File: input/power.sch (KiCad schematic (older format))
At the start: 61 parts, among them Q2 2STD1665T4, Q3 NSS1C300ET4G, U4 OPA830, U6 OPA830, U7 MCP1755S-3302E/DB, U8 NCP1117STAT3G

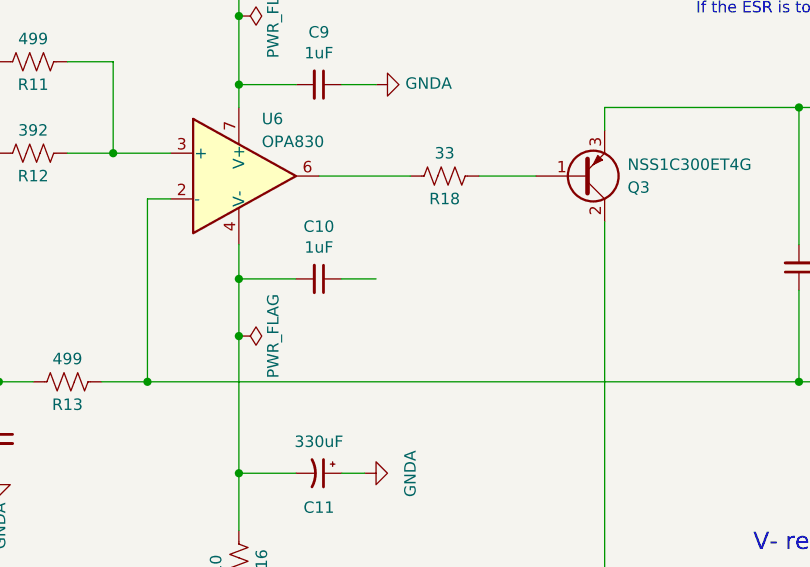
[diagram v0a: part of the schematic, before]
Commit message: Input board is nearly ready to send off for the first spin.
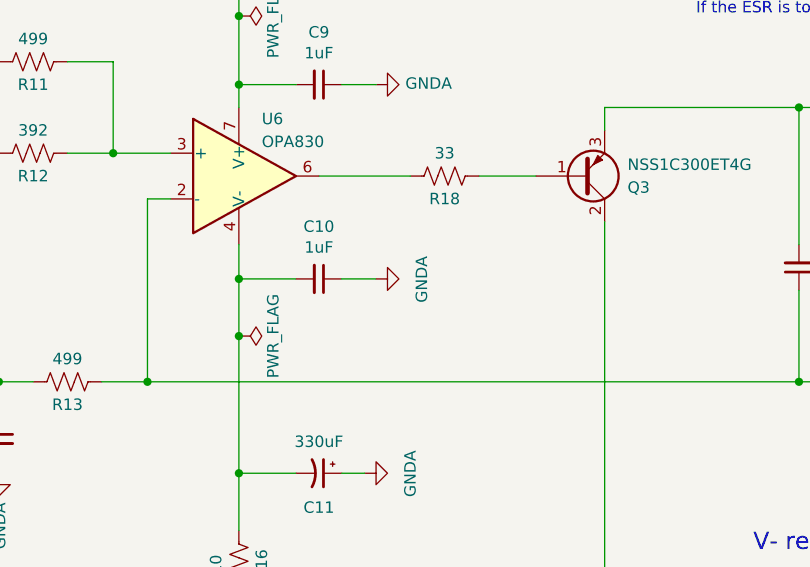
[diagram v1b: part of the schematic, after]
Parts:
- TP4: DK line (none) -> 33; Description (none) -> TERM TURRET HOLLOW L=6.75MM TIN; Digikey (none) -> 36-1540-2-ND; MPN (none) -> 1540-2; Manufacturer (none) -> Keystone Electronics
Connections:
- net GND: now also C10.1
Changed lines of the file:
@@
 $Descr B 17000 11000
 encoding utf-8
-Sheet 11 21
+Sheet 4 21
 Title ""
 Date ""
@@
 F 2 "input:TestPoint_THTPad_D5.0mm_Drill2.41mm" H 2950 8300 50  0001 C CNN
 F 3 "~" H 2950 8300 50  0001 C CNN
+F 4 "33" H 2750 8300 50  0001 C CNN "DK line"
+F 5 "TERM TURRET HOLLOW L=6.75MM TIN" H 2750 8300 50  0001 C CNN "Description"
+F 6 "36-1540-2-ND" H 2750 8300 50  0001 C CNN "Digikey"
+F 7 "1540-2" H 2750 8300 50  0001 C CNN "MPN"
+F 8 "Keystone Electronics" H 2750 8300 50  0001 C CNN "Manufacturer"
 	1    2750 8300
 	1    0    0    -1
@@
 Wire Wire Line
 	7250 2100 7350 2100
+$Comp
+L power:GNDA #PWR?
+U 1 1 5E478F7A
+P 9250 6000
+AR Path="/5DFF6C0D/5E478F7A" Ref="#PWR?"  Part="1"
+AR Path="/5E1D6729/5E1DA2AA/5E478F7A" Ref="#PWR?"  Part="1"
+AR Path="/5E2EB92B/5E478F7A" Ref="#PWR?"  Part="1"
+AR Path="/5E51E83D/5E478F7A" Ref="#PWR0166"  Part="1"
+F 0 "#PWR0166" H 9250 5750 50  0001 C CNN
+F 1 "GNDA" H 9350 5800 50  0000 R CNN
+F 2 "" H 9250 6000 50  0001 C CNN
+F 3 "" H 9250 6000 50  0001 C CNN
+	1    9250 6000
+	0    -1   -1   0
+$EndComp
 $EndSCHEMATC

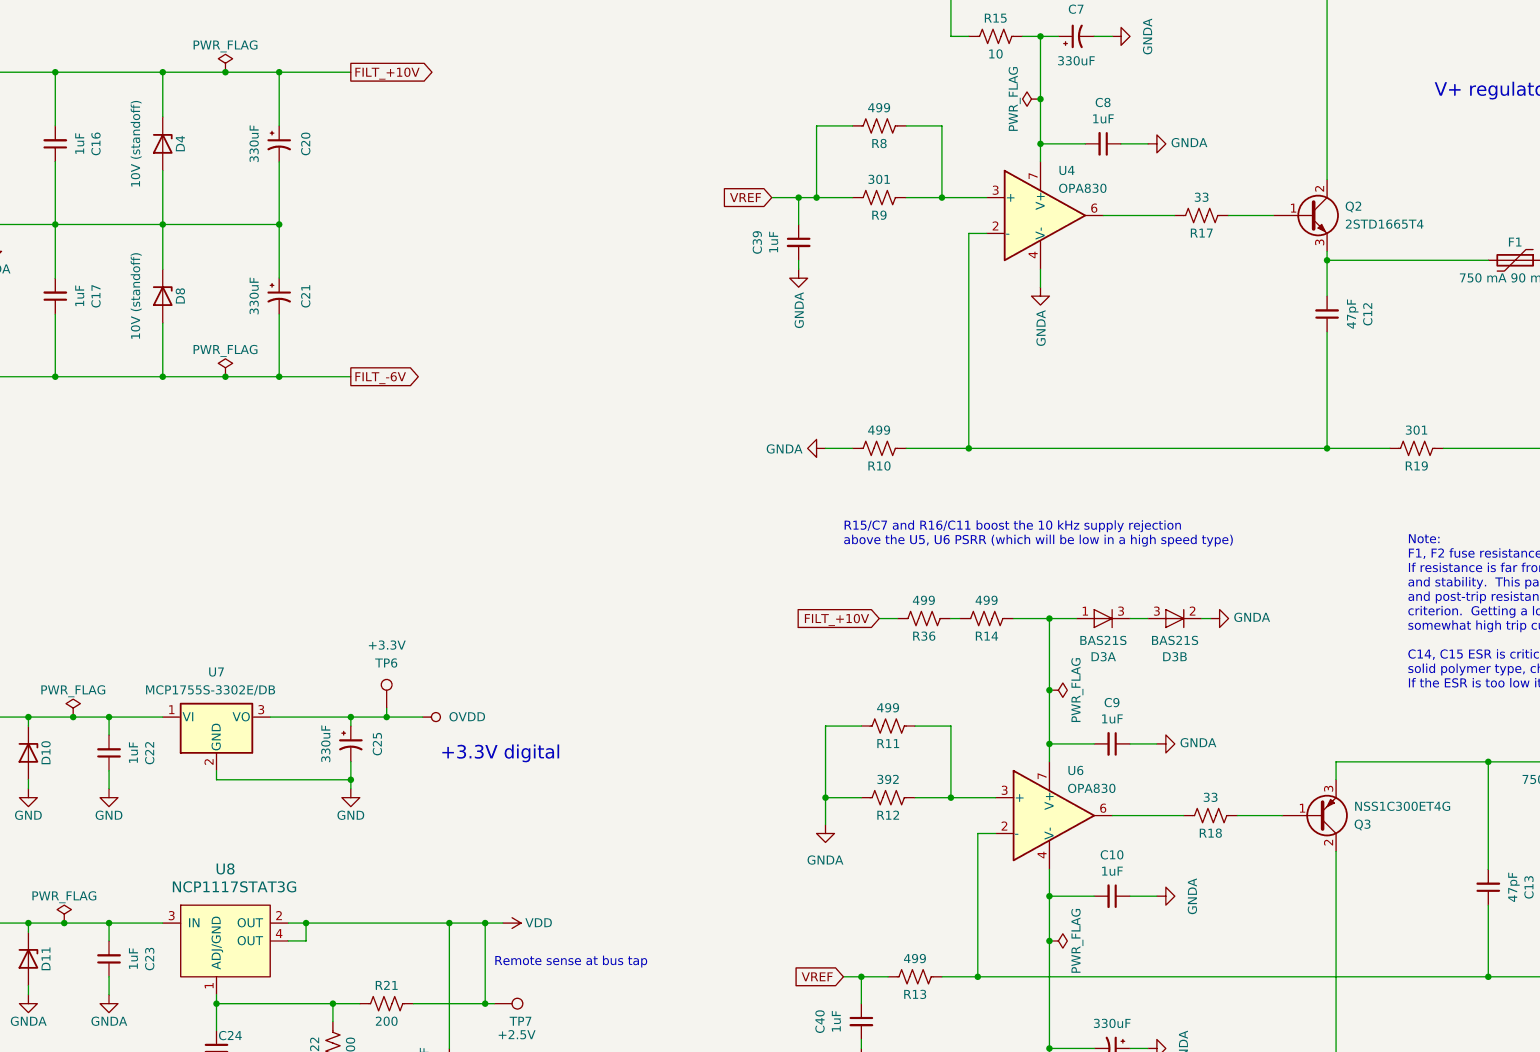
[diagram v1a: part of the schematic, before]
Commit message: Various tweaks to schematic which help in the PCB view, mainly getting informative net names. Also unscrambled the + and - paths in the input channel.  This avoided a cross-over before the first stage, and an unintended inversion, but mostly just made net naming less confusing.
Getting better net names made it easier to review the PCB to see if it made sense.  I checked
the ICs on the PCB against the datasheet pinout, and while doing this fixed an actual bug where
I had BIST-+ and BIST+-swapped.

I made some tweaks on the PCB to try to equalize the copper area on the input nets so as to
match the capacitance.  I tweaked the top-side ground pours somewhat, adding in the regulator
area, removing around the high speed traces.

Some changes from gerber viewing.  I reduced the solder mask clearances so that we get mask
web between the SOIC and DFN pads.  I reduced the pad size of the big via from 1.2 to 1.0 mm.
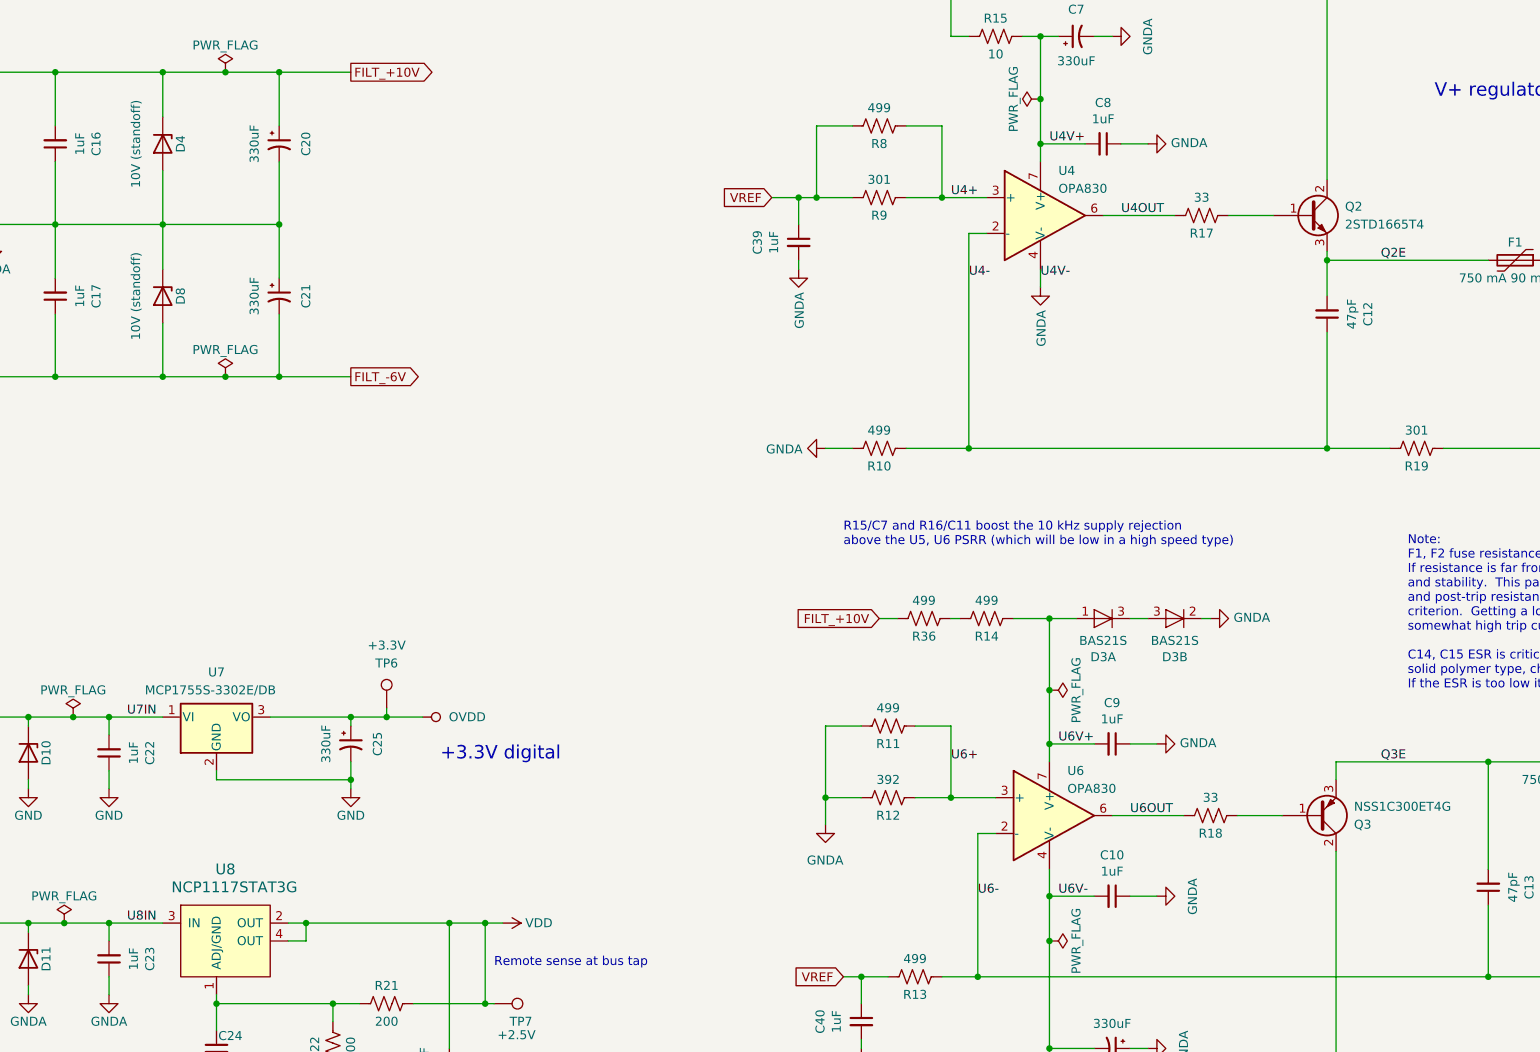
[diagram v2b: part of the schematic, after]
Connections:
- net U6V+: now reaches C9.2, D3.1 (A), R14.1, U6.7 (V+)
- net U8IN: now reaches C23.2, D11.1 (K), FB4.2, U8.3 (IN)
- net U7IN: now reaches C22.2, D10.1 (K), FB3.2, U7.1 (VI)
- net U6-: now reaches C13.1, R13.1, R20.2, U6.2 (-)
- net Q3E: now reaches C13.2, F2.2, Q3.3 (E)
- net U6+: now reaches R11.1, R12.1, U6.3 (+)
- net U6V-: now reaches C10.2, C11.2, R16.1, U6.4 (V-)
- net U6OUT: now reaches R18.2, U6.6
- net U4V+: now reaches C7.1, C8.2, R15.2, U4.7 (V+)
- net U4-: now reaches C12.1, R10.1, R19.2, U4.2 (-)
- net U4+: now reaches R8.1, R9.1, U4.3 (+)
- net U4OUT: now reaches R17.2, U4.6
- net Q2E: now reaches C12.2, F1.2, Q2.3 (E)
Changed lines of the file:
@@
 F 1 "BAS21S" H 8950 4574 50  0000 C CNN
 F 2 "Package_TO_SOT_SMD:SOT-23" H 8950 4300 50  0001 C CNN
-F 3 "https://assets.nexperia.com/documents/data-sheet/BAV99_SER.pdf" H 8950 4550 50  0001 C CNN
+F 3 "http://www.onsemi.com/pub/Collateral/BAS21SLT1-D.PDF" H 8950 4550 50  0001 C CNN
 F 4 "43" H 8950 4450 50  0001 C CNN "DK line"
 F 5 "DIODE ARRAY GP 250V 225MA SOT23" H 8950 4450 50  0001 C CNN "Description"
@@
 F 1 "BAS21S" H 9350 4574 50  0000 C CNN
 F 2 "Package_TO_SOT_SMD:SOT-23" H 9350 4300 50  0001 C CNN
-F 3 "https://assets.nexperia.com/documents/data-sheet/BAV99_SER.pdf" H 9350 4550 50  0001 C CNN
+F 3 "http://www.onsemi.com/pub/Collateral/BAS21SLT1-D.PDF" H 9350 4550 50  0001 C CNN
 F 4 "43" H 9350 4450 50  0001 C CNN "DK line"
 F 5 "DIODE ARRAY GP 250V 225MA SOT23" H 9350 4450 50  0001 C CNN "Description"
@@
 	0    -1   -1   0
 $EndComp
+Text Label 8250 6000 0    50   ~ 0
+U6-
+Text Label 8100 5250 0    50   ~ 0
+U6+
+Text Label 9100 5550 0    50   ~ 0
+U6OUT
+Text Label 8700 5150 0    50   ~ 0
+U6V+
+Text Label 8700 6000 0    50   ~ 0
+U6V-
+Text Label 9050 2200 0    50   ~ 0
+U4OUT
+Text Label 8600 2550 0    50   ~ 0
+U4V-
+Text Label 8650 1800 0    50   ~ 0
+U4V+
+Text Label 8200 2550 0    50   ~ 0
+U4-
+Text Label 8100 2100 0    50   ~ 0
+U4+
+Text Label 10500 2450 0    50   ~ 0
+Q2E
+Text Label 10500 5250 0    50   ~ 0
+Q3E
+Text Label 3500 5000 0    50   ~ 0
+U7IN
+Text Label 3500 6150 0    50   ~ 0
+U8IN
 $EndSCHEMATC

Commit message: Work on main board.
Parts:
- renumbered D10 to D?, D11 to D?, F2 to F?, F1 to F?, U8 to U?, U7 to U?

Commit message: Checkpoint of state before I start schematic revisions for the next version of the input board. There are not any substantive modifications to the input board, but some broad changes in component attributes related enabling a fabrication quote.
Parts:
- C10, C16, C17, C22, C23, C39, C40, C8, C9: Manufacturer (none) -> Samsung Electro-Mechanics
- C11, C14, C15, C20, C21, C25, C26, C7: Manufacturer (none) -> United Chemi-Con
- C12, C13: MPN (none) -> CC0603JRNPO9BN470; Manufacturer (none) -> Yageo
- C24: Manufacturer (none) -> AVX Corporation
- C32: Manufacturer (none) -> Murata Electronics
- D10, D11: renamed from D?; Manufacturer (none) -> Würth Elektronik
- D15, D16, D4, D8: Manufacturer (none) -> Würth Elektronik
- D3: Manufacturer (none) -> ON Semiconductor
- F1, F2: renamed from F?; Manufacturer (none) -> Bel Fuse Inc.
- FB1, FB2, FB3, FB4: MPN HZ0805C202R-10 -> FBMJ2125HM210NT; Manufacturer (none) -> Taiyo Yuden
- Q2: MPN (none) -> 2STD1665T4; Manufacturer (none) -> STMicroelectronics
- Q3: MPN (none) -> NSS1C300ET4G; Manufacturer (none) -> ON Semiconductor
- R10, R11, R13, R14, R36, R8: MPN (none) -> 8-2176091-9; Manufacturer (none) -> TE Connectivity Passive Product
- R12, R20: MPN (none) -> RNCP0603FTD392R; Manufacturer (none) -> Stackpole Electronics Inc
- R15, R16: Manufacturer (none) -> Vishay Dale
- R17, R18: Description (none) -> RES 33 OHM 1% 1/10W 0603; MPN (none) -> RMCF0603FT33R0; Manufacturer (none) -> Stackpole Electronics Inc
- R19, R9: MPN (none) -> RNCP0603FTD301R; Manufacturer (none) -> Stackpole Electronics Inc
- R21, R22: MPN (none) -> RNCP0603FTD200R; Manufacturer (none) -> Stackpole Electronics Inc
- TP6, TP7, TP8, TP9: Description (none) -> Do Not Populate; MPN (none) -> DNP
- U4, U6: MPN (none) -> OPA830ID; Manufacturer (none) -> Texas Instruments
- U7: renamed from U?; MPN (none) -> MCP1755S-3302E/DB; Manufacturer (none) -> Microchip Technology
- gave numbers to parts that had none: 1
